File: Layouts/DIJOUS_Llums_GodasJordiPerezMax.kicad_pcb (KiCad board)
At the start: 2 copper layers, 85.1 x 69 mm, 104 parts, among them J1 Conn_01x05_Socket, J2 Conn_01x03, J3 Conn_01x06, J4 Screw_Terminal_01x02, J5 Conn_01x05, J6 DE9_Plug, J7 Conn_01x02, J8 Conn_01x06_Socket, K1 G5LE-1 DC12, K2 G5LE-1 DC12, Q1 ZXTN19020DFFTA, Q2 ZXTN19020DFFTA, Q3 ZXTN19020DFFTA, Q4 Si7336ADP, Q5 Si7336ADP, Q6 ZXTN19020DFFTA, Q7 ZXTN19020DFFTA, Q8 Si7336ADP, Q9 Si7336ADP, U1 PCA9306D, U2 PIC18F2580-I/SO, U3 LM2596T-ADJ, U4 LT1117-5.0, U5 MCP2551-I-SN, U7 LT6202CS5, U8 TLV1117-33

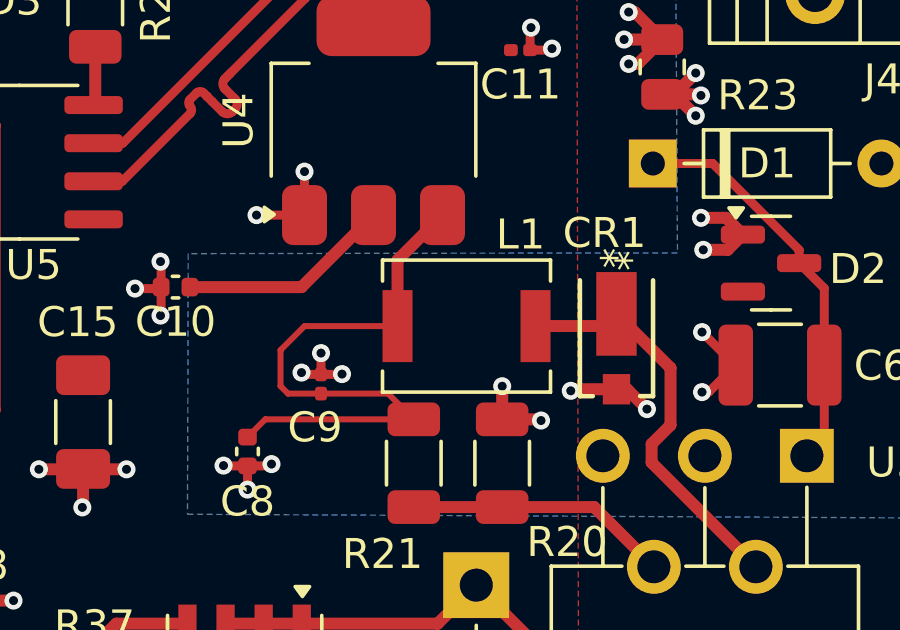
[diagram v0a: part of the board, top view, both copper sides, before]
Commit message: Ruteado footprint bobina
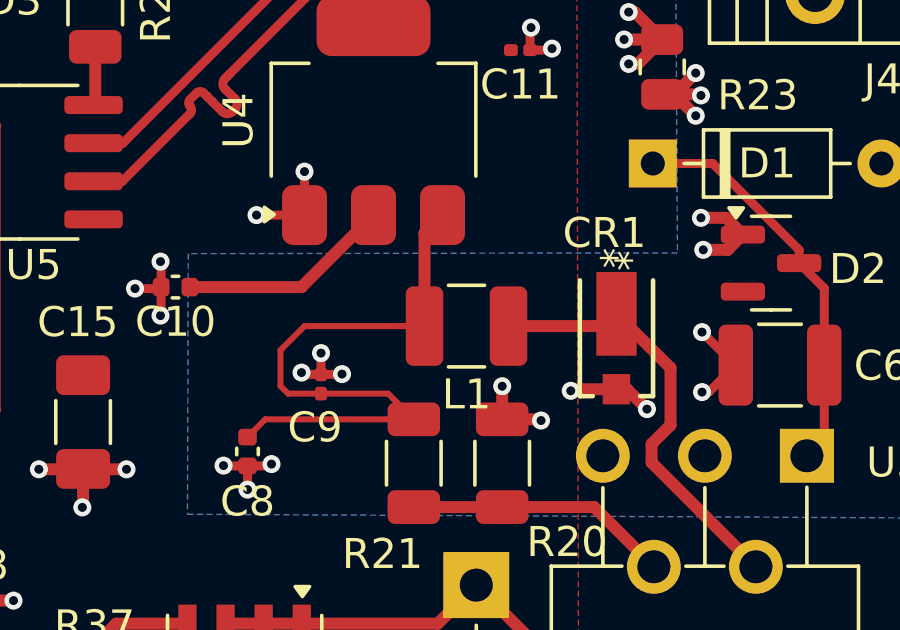
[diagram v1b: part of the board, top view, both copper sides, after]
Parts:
- L1: footprint Inductor_SMD:L_Neosid_Ms42 -> Inductor_SMD:L_1210_3225Metric
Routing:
- net /Buck_OUT: track 13.3 -> 14.6 mm
- net /LDO5V_IN: track 20.8 -> 22.1 mm
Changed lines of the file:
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@@
 		)
 	)
-	(footprint "Inductor_SMD:L_Neosid_Ms42"
+	(footprint "Inductor_SMD:L_1210_3225Metric"
 		(layer "F.Cu")
 		(at 125.1 53.85 180)
-		(descr "Neosid, Inductor, SMs42, Fixed inductor, SMD, magneticaly shielded, https://neosid.de/import-data/product-pdf/neoFestind_Ms42.pdf")
-		(tags "Neosid Inductor SMs42 Fixed inductor SMD magneticaly shielded")
+		(descr "Inductor SMD 1210 (3225 Metric), square (rectangular) end terminal, IPC_7351 nominal, (Body size source: http://www.tortai-tech.com/upload/download/2011102023233369053.pdf), generated with kicad-footprint-generator")
+		(tags "inductor")
 		(property "Reference" "L1"
-			(at -1.8 3.05 0)
+			(at 0 -2.28 180)
 			(layer "F.SilkS")
 			(effects
@@
 		)
 		(property "Value" "47uH"
-			(at 0 3.1 0)
+			(at 0 2.28 180)
 			(layer "F.Fab")
 			(effects
@@
 			)
 		)
-		(property "Footprint" "Inductor_SMD:L_Neosid_Ms42"
+		(property "Footprint" "Inductor_SMD:L_1210_3225Metric"
 			(at 0 0 180)
 			(unlocked yes)
@@
 		(attr smd)
 		(fp_line
-			(start 2.8 2.2)
-			(end -2.8 2.2)
+			(start -0.602064 1.36)
+			(end 0.602064 1.36)
 			(stroke
 				(width 0.12)
@@
 		)
 		(fp_line
-			(start 2.8 1.5)
-			(end 2.8 2.2)
+			(start -0.602064 -1.36)
+			(end 0.602064 -1.36)
 			(stroke
 				(width 0.12)
@@
 		)
 		(fp_line
-			(start 2.8 -2.2)
-			(end 2.8 -1.5)
-			(stroke
-				(width 0.12)
-				(type solid)
-			)
-			(layer "F.SilkS")
-		)
-		(fp_line
-			(start 2.8 -2.2)
-			(end -2.8 -2.2)
-			(stroke
-				(width 0.12)
-				(type solid)
-			)
-			(layer "F.SilkS")
-		)
-		(fp_line
-			(start -2.8 2.2)
-			(end -2.8 1.5)
-			(stroke
-				(width 0.12)
-				(type solid)
-			)
-			(layer "F.SilkS")
-		)
-		(fp_line
-			(start -2.8 -2.2)
-			(end -2.8 -1.5)
-			(stroke
-				(width 0.12)
-				(type solid)
-			)
-			(layer "F.SilkS")
-		)
-		(fp_line
-			(start 3.05 2.25)
-			(end 3.05 -2.25)
+			(start 2.28 1.58)
+			(end -2.28 1.58)
 			(stroke
 				(width 0.05)
@@
 		)
 		(fp_line
-			(start 3.05 2.25)
-			(end -3.05 2.25)
+			(start 2.28 -1.58)
+			(end 2.28 1.58)
 			(stroke
 				(width 0.05)
@@
 		)
 		(fp_line
-			(start -3.05 -2.25)
-			(end 3.05 -2.25)
+			(start -2.28 1.58)
+			(end -2.28 -1.58)
 			(stroke
 				(width 0.05)
@@
 		)
 		(fp_line
-			(start -3.05 -2.25)
-			(end -3.05 2.25)
+			(start -2.28 -1.58)
+			(end 2.28 -1.58)
 			(stroke
 				(width 0.05)
@@
 		)
 		(fp_line
-			(start 2.8 1)
-			(end 2 1)
-			(stroke
-				(width 0.1)
-				(type solid)
-			)
-			(layer "F.Fab")
-		)
-		(fp_line
-			(start 2.8 -1)
-			(end 2.8 1)
-			(stroke
-				(width 0.1)
-				(type solid)
-			)
-			(layer "F.Fab")
-		)
-		(fp_line
-			(start 2 2)
-			(end -2 2)
-			(stroke
-				(width 0.1)
-				(type solid)
-			)
-			(layer "F.Fab")
-		)
-		(fp_line
-			(start 2 -1)
-			(end 2.8 -1)
-			(stroke
-				(width 0.1)
-				(type solid)
-			)
-			(layer "F.Fab")
-		)
-		(fp_line
-			(start 2 -2)
-			(end 2 2)
-			(stroke
-				(width 0.1)
-				(type solid)
-			)
-			(layer "F.Fab")
-		)
-		(fp_line
-			(start -2 2)
-			(end -2 -2)
+			(start 1.6 1.25)
+			(end -1.6 1.25)
 			(stroke
 				(width 0.1)
@@
 		)
 		(fp_line
-			(start -2 1)
-			(end -2.8 1)
+			(start 1.6 -1.25)
+			(end 1.6 1.25)
 			(stroke
 				(width 0.1)
@@
 		)
 		(fp_line
-			(start -2 -2)
-			(end 2 -2)
+			(start -1.6 1.25)
+			(end -1.6 -1.25)
 			(stroke
 				(width 0.1)
@@
 		)
 		(fp_line
-			(start -2.8 1)
-			(end -2.8 -1)
-			(stroke
-				(width 0.1)
-				(type solid)
-			)
-			(layer "F.Fab")
-		)
-		(fp_line
-			(start -2.8 -1)
-			(end -2 -1)
+			(start -1.6 -1.25)
+			(end 1.6 -1.25)
 			(stroke
 				(width 0.1)
@@
 		)
 		(fp_text user "${REFERENCE}"
-			(at 0 0 0)
+			(at 0 0 180)
 			(layer "F.Fab")
 			(effects
 				(font
-					(size 1 1)
-					(thickness 0.15)
+					(size 0.8 0.8)
+					(thickness 0.12)
 				)
 			)
 		)
-		(pad "1" smd rect
-			(at -2.3 0 180)
-			(size 1 2.4)
+		(pad "1" smd roundrect
+			(at -1.4 0 180)
+			(size 1.25 2.65)
 			(layers "F.Cu" "F.Paste" "F.Mask")
+			(roundrect_rratio 0.2)
 			(net 8 "/Buck_OUT")
 			(pinfunction "1")
 			(pintype "passive")
 		)
-		(pad "2" smd rect
-			(at 2.3 0 180)
-			(size 1 2.4)
+		(pad "2" smd roundrect
+			(at 1.4 0 180)
+			(size 1.25 2.65)
 			(layers "F.Cu" "F.Paste" "F.Mask")
+			(roundrect_rratio 0.2)
 			(net 7 "/LDO5V_IN")
 			(pinfunction "2")
 			(pintype "passive")
 		)
-		(model "${KICAD8_3DMODEL_DIR}/Inductor_SMD.3dshapes/L_Neosid_Ms42.wrl"
+		(model "${KICAD8_3DMODEL_DIR}/Inductor_SMD.3dshapes/L_1210_3225Metric.wrl"
 			(offset
 				(xyz 0 0 0)
@@
 	(segment
 		(start 119.7 53.85)
-		(end 122.8 53.85)
+		(end 118.9 54.65)
 		(width 0.2)
 		(layer "F.Cu")
@@
 	)
 	(segment
-		(start 122.8 53.85)
-		(end 122.8 51.65)
-		(width 0.4)
-		(layer "F.Cu")
-		(net 7)
-	)
-	(segment
-		(start 122.8 51.65)
-		(end 124.3 50.15)
+		(start 123.7 53.85)
+		(end 123.7 50.75)
 		(width 0.4)
 		(layer "F.Cu")
@@
 	)
 	(segment
-		(start 122.6964 53.7464)
-		(end 122.8 53.85)
+		(start 123.157899 57.142001)
+		(end 123.3424 56.9575)
 		(width 0.2)
 		(layer "F.Cu")
@@
 	)
 	(segment
-		(start 123.157899 57.142001)
-		(end 123.3424 56.9575)
+		(start 122.8 53.85)
+		(end 123.7 53.85)
 		(width 0.2)
 		(layer "F.Cu")
@@
 	)
 	(segment
-		(start 118.9 55.85)
-		(end 118.9 54.65)
+		(start 123.3424 56.9575)
+		(end 118.3925 56.9575)
 		(width 0.2)
 		(layer "F.Cu")
@@
 	)
 	(segment
-		(start 123.3424 56.9575)
-		(end 118.3925 56.9575)
+		(start 123.7 50.75)
+		(end 124.3 50.15)
+		(width 0.4)
+		(layer "F.Cu")
+		(net 7)
+	)
+	(segment
+		(start 118.9 54.65)
+		(end 118.9 55.85)
 		(width 0.2)
 		(layer "F.Cu")
@@
 	)
 	(segment
-		(start 119.15 56.1)
+		(start 122.4849 56.1)
 		(end 120.25 56.1)
 		(width 0.2)
@@
 	)
 	(segment
-		(start 118.9 54.65)
-		(end 119.7 53.85)
+		(start 119.15 56.1)
+		(end 120.25 56.1)
 		(width 0.2)
 		(layer "F.Cu")
@@
 	)
 	(segment
-		(start 122.4849 56.1)
-		(end 120.25 56.1)
+		(start 123.7 53.85)
+		(end 119.7 53.85)
 		(width 0.2)
 		(layer "F.Cu")
@@
 	)
 	(segment
-		(start 130.0988 53.4432)
-		(end 131.9 55.2444)
+		(start 129.692 53.85)
+		(end 130.0988 53.4432)
 		(width 0.4)
 		(layer "F.Cu")
@@
 	)
 	(segment
-		(start 131.9 55.2444)
-		(end 131.9 57.15)
+		(start 130.0988 53.4432)
+		(end 131.9 55.2444)
 		(width 0.4)
 		(layer "F.Cu")
@@
 	)
 	(segment
-		(start 129.694 53.848)
-		(end 130.0988 53.4432)
+		(start 131.9 55.2444)
+		(end 131.9 57.15)
 		(width 0.4)
 		(layer "F.Cu")
@@
 	)
 	(segment
-		(start 127.8776 53.848)
-		(end 129.694 53.848)
+		(start 126.5 53.85)
+		(end 129.692 53.85)
 		(width 0.4)
 		(layer "F.Cu")
